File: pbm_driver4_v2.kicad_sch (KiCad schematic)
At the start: 14 parts, among them J1 Conn_02x10_Odd_Even, J2 Conn_01x10

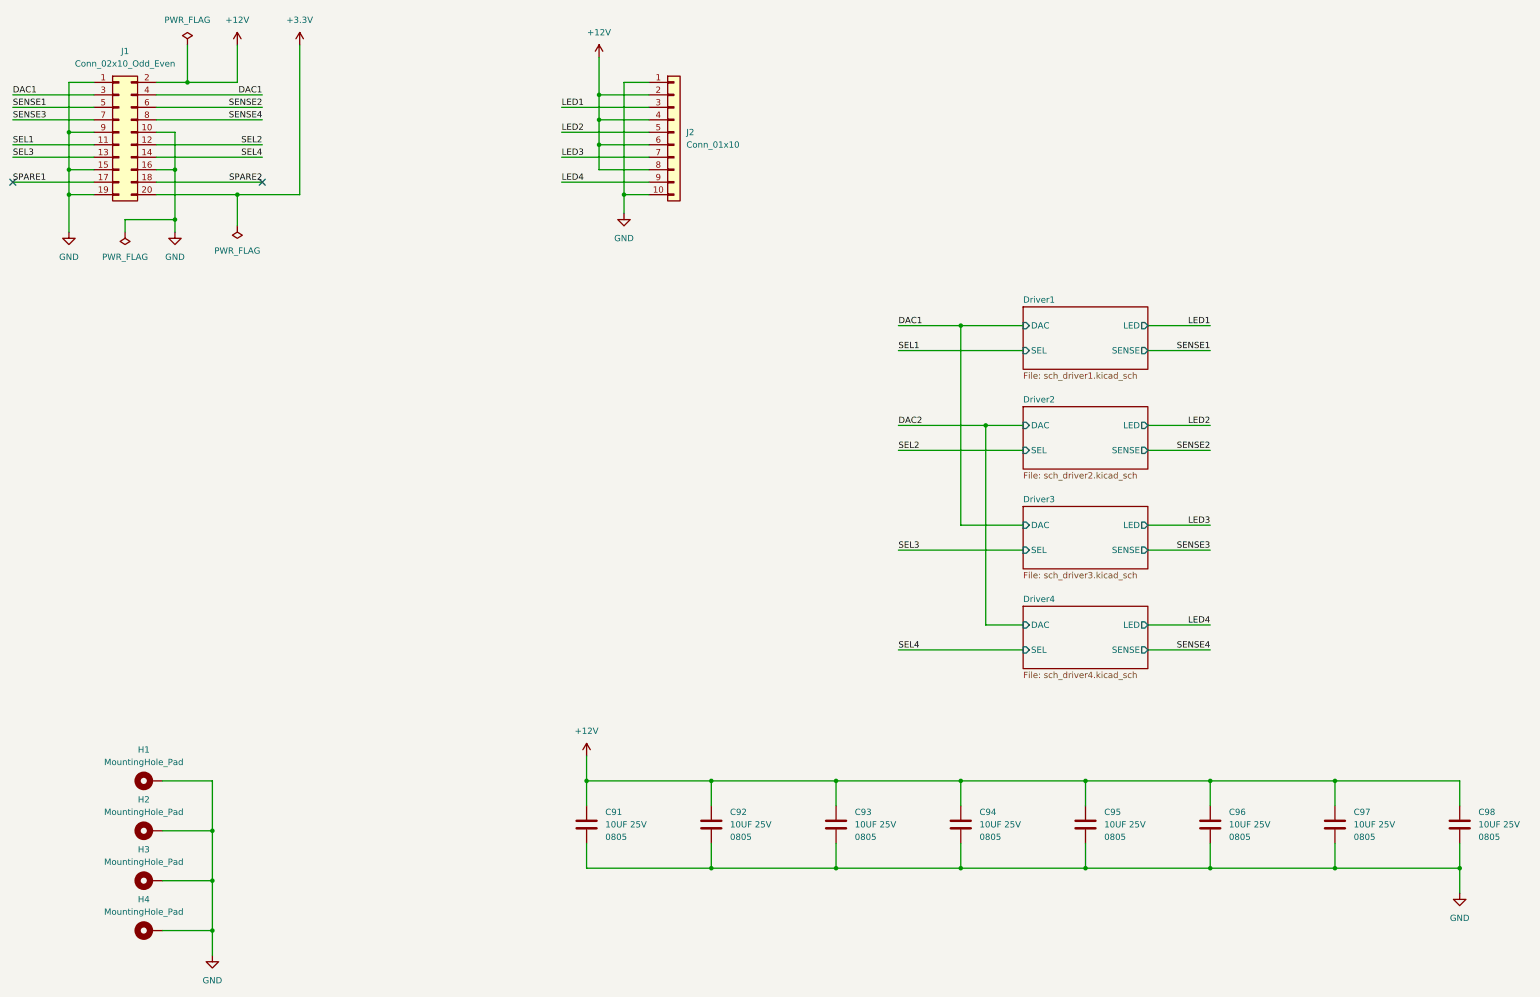
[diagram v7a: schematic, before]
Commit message: Finished schematic refactor to six A-sheets. Updated PCB.
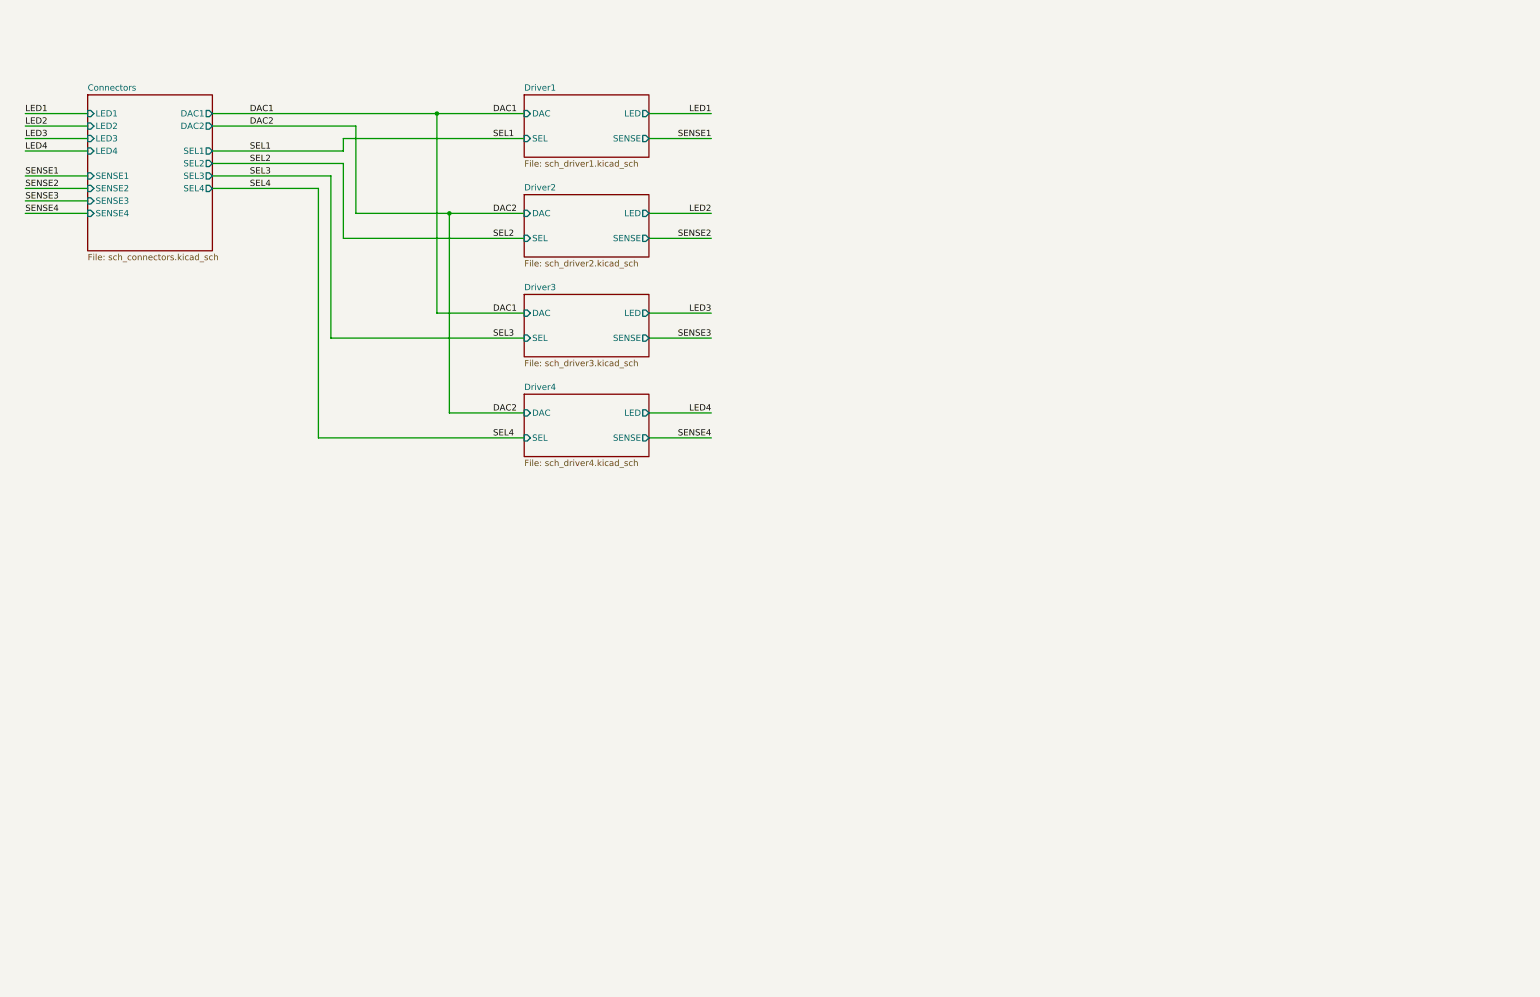
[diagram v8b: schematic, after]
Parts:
- removed C91, C92, C93, C94, C95, C96, C97, C98: 10UF 25V, $Local:C_0805_2012Metric, symbol $Local:C_0805_10UF_25V
- removed H1, H2, H3, H4: MountingHole_Pad, $Local:MountingHole_3.2mm_M3_Pad, symbol $Local:MountingHole_Pad
- removed J1: Conn_02x10_Odd_Even, $Local:PinHeader_2x10_P2.54mm_Vertical, symbol $Local:Conn_02x10_Odd_Even
- removed J2: Conn_01x10, $Local:PinHeader_1x10_P2.54mm_Vertical, symbol $Local:Conn_01x10
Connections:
- no-connect marks 2 -> 0
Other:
- added sheet Connectors (sch_connectors.kicad_sch)
